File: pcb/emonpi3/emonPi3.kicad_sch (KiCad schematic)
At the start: 133 parts, among them CN1 CONN_03SCREW, CN2 CONN_03SCREW, CN3 CONN_03SCREW, J10 Conn_ARM_JTAG_SWD_10, J11 Conn_02x13_Odd_Even, J12 PINHD-1X9, J7 CONN_04PTH, J8 CONN_04PTH, J9 USB_C_Receptacle_USB2.0, SW1 SW_Push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

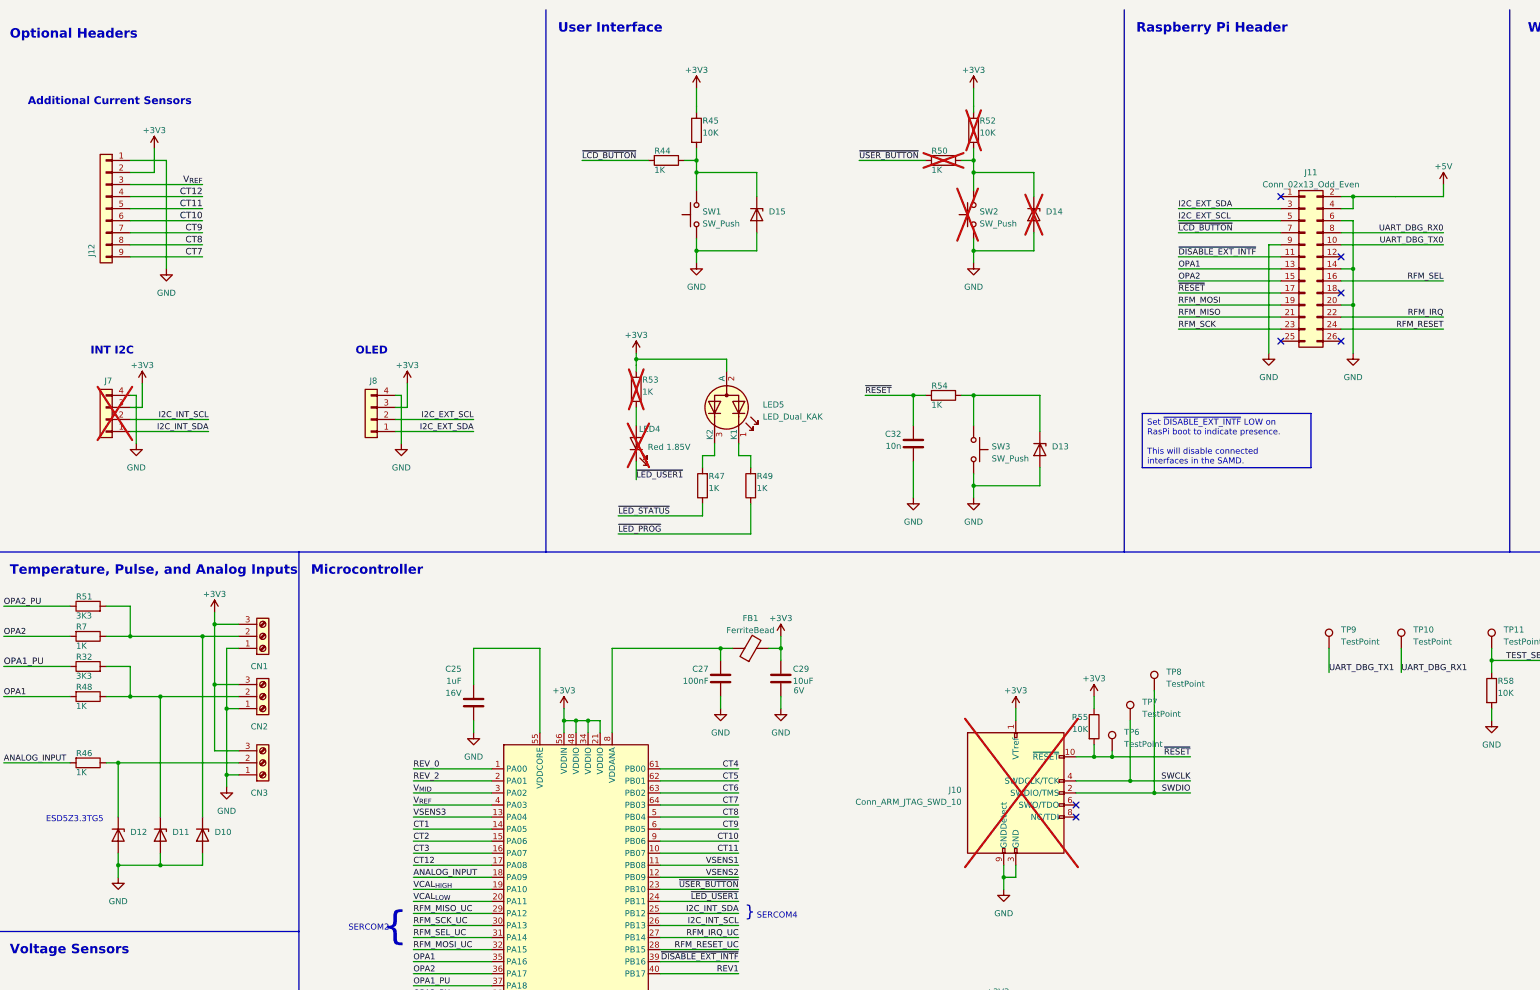
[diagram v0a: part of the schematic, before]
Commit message: * [Header] Use 40 pin RasPi header and move 6CT header
  - Use a 40 pin header for RasPi
  - Move 6CT (and change pinout) to allow this
  - Use routing mapping for CT inputs, do remap in software
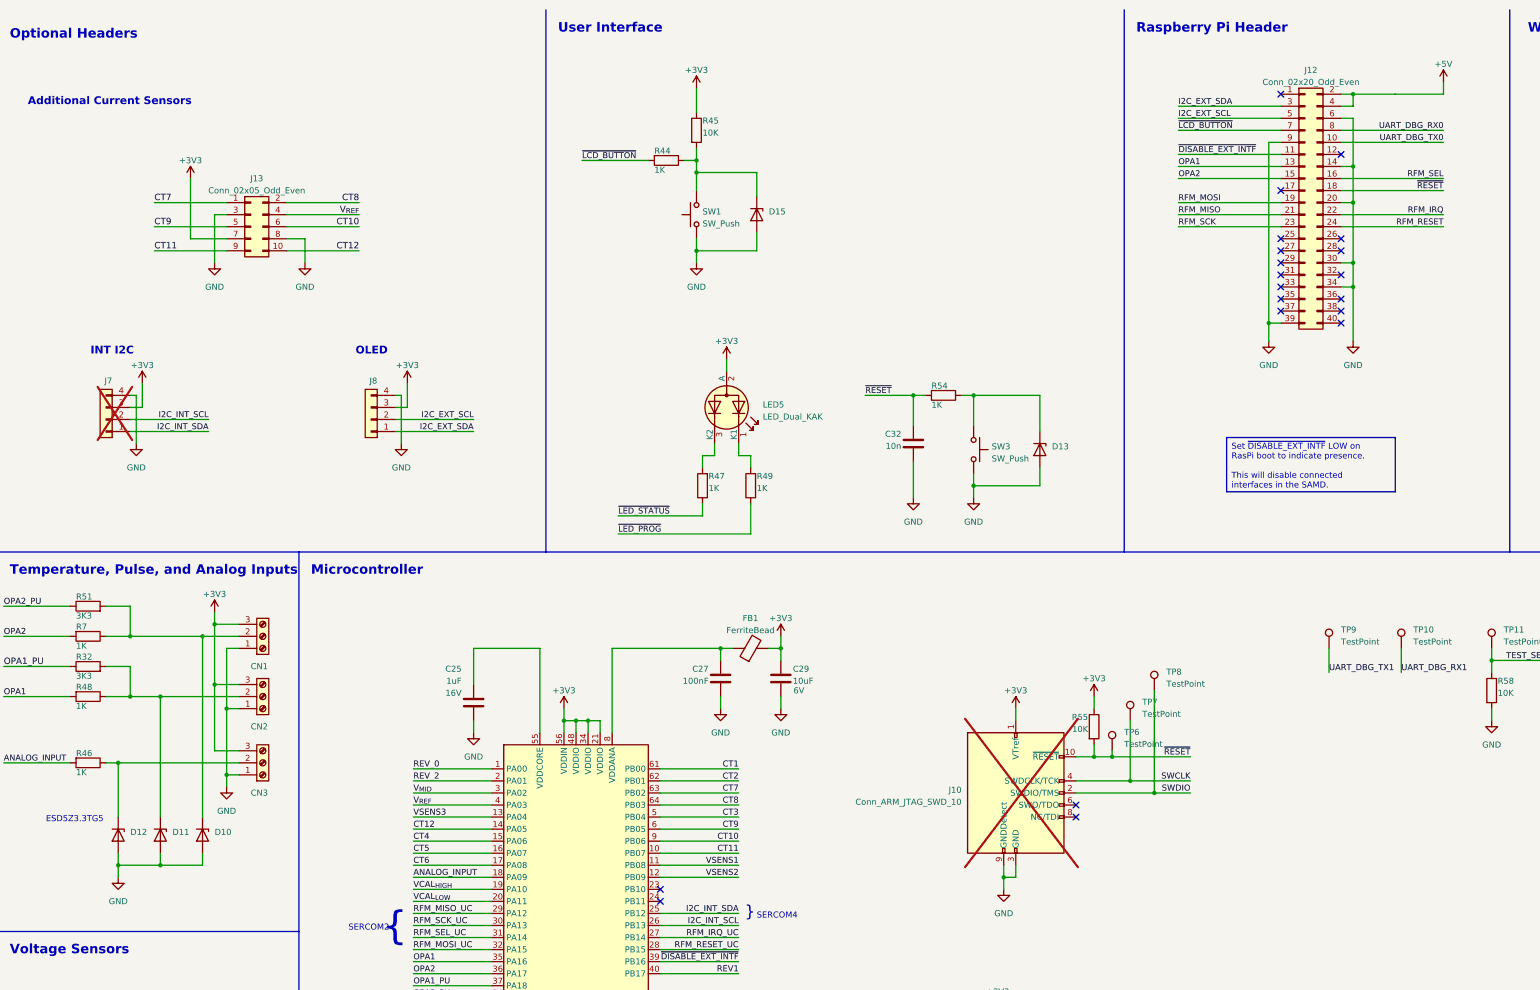
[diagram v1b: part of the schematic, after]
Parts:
- removed D14: ESD5Z3.3T5G, Diode_SMD:D_SOD-523, symbol Diode:ESD5Zxx
- removed J11: Conn_02x13_Odd_Even, RPi-SMD:REF-182688, symbol Connector_Generic:Conn_02x13_Odd_Even
- removed J12: PINHD-1X9, Connector_PinSocket_2.54mm:PinSocket_1x09_P2.54mm_Vertical, symbol Connector_Generic:Conn_01x09
- removed LED4: Red 1.85V, LED_SMD:LED_0805_2012Metric, symbol Device:LED
- removed R50, R53: 1K, Resistor_SMD:R_0603_1608Metric, symbol Device:R
- removed R52: 10K, Resistor_SMD:R_0603_1608Metric, symbol Device:R
- removed SW2: SW_Push, Button_Switch_THT:SW_PUSH_6mm, symbol Switch:SW_Push
- added J12: Conn_02x20_Odd_Even, RPi-SMD:REF-182665, symbol Connector_Generic:Conn_02x20_Odd_Even
- added J13: Conn_02x05_Odd_Even, Connector_PinSocket_2.54mm:PinSocket_2x05_P2.54mm_Vertical, symbol Connector_Generic:Conn_02x05_Odd_Even
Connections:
- net +3V3: now also J13.7 (Pin_7)
- net +5V: now also J12.2 (Pin_2), J12.4 (Pin_4)
- net CT1: now also U3.61 (PB00); no longer U3.14 (PA05)
- net CT10: now also J13.6 (Pin_6)
- net CT11: now also J13.9 (Pin_9)
- net CT12: now also U3.14 (PA05), J13.10 (Pin_10); no longer U3.17 (PA08)
- net CT2: now also U3.62 (PB01); no longer U3.15 (PA06)
- net CT3: now also U3.5 (PB04); no longer U3.16 (PA07)
- net CT4: now also U3.15 (PA06); no longer U3.61 (PB00)
- net CT5: now also U3.16 (PA07); no longer U3.62 (PB01)
- net CT6: now also U3.17 (PA08); no longer U3.63 (PB02)
- net CT7: now also U3.63 (PB02), J13.1 (Pin_1); no longer U3.64 (PB03)
- net CT8: now also U3.64 (PB03), J13.2 (Pin_2); no longer U3.5 (PB04)
- net CT9: now also J13.5 (Pin_5)
- net GND: now also J12.14 (Pin_14), J12.20 (Pin_20), J12.30 (Pin_30), J12.34 (Pin_34), J12.39 (Pin_39), J12.6 (Pin_6), J12.9 (Pin_9), J13.3 (Pin_3), J13.8 (Pin_8)
- net I2C_EXT_SCL: now also J12.5 (Pin_5)
- net I2C_EXT_SDA: now also J12.3 (Pin_3)
- net OPA1: now also J12.13 (Pin_13)
- net OPA2: now also J12.15 (Pin_15)
- net RFM_IRQ: now also J12.22 (Pin_22)
- net RFM_MISO: now also J12.21 (Pin_21)
- net RFM_MOSI: now also J12.19 (Pin_19)
- net RFM_RESET: now also J12.24 (Pin_24)
- net RFM_SCK: now also J12.23 (Pin_23)
- net RFM_SEL: now also J12.16 (Pin_16)
- net UART_DBG_RX0: now also J12.8 (Pin_8)
- net UART_DBG_TX0: now also J12.10 (Pin_10)
- net V_{REF}: now also J13.4 (Pin_4)
- net ~{DISABLE_EXT_INTF}: now also J12.11 (Pin_11)
- net ~{LCD_BUTTON}: now also J12.7 (Pin_7)
- net ~{RESET}: now also J12.18 (Pin_18)
- net ~{LED_USER1}: no longer names the net of U3.24 (PB11)
- net ~{USER_BUTTON}: no longer names the net of U3.23 (PB10)
- no-connect marks 14 -> 27

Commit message: * Changes for manufacture
  - Better silkscreen naming
  - Move test points to top layer and remove alignment holes
  - Remove additional UART pads
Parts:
- removed CN1, CN2: CONN_03SCREW, TerminalBlock_Phoenix:TerminalBlock_Phoenix_PT-1,5-3-3.5-H_1x03_P3.50mm_Horizontal, symbol Connector:Screw_Terminal_01x03
- removed H5, H6: MountingHole, MountingHole:MountingHole_2.1mm, symbol Mechanical:MountingHole
- removed R58: 10K, Resistor_SMD:R_0603_1608Metric, symbol Device:R
- removed TP10, TP11, TP7, TP8, TP9: TestPoint, TestPoint:TestPoint_Pad_D1.0mm, symbol Connector:TestPoint
- added CN1: Screw_Terminal_01x06, TerminalBlock_Phoenix:TerminalBlock_Phoenix_PT-1,5-6-3.5-H_1x06_P3.50mm_Horizontal, symbol Connector:Screw_Terminal_01x06
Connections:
- net +3V3: now also CN1.3 (Pin_3), CN1.6 (Pin_6)
- net GND: now also TP6.1, CN1.1 (Pin_1), CN1.4 (Pin_4)
- net ~{RESET}: no longer TP6.1
- net at D10.1 (K), R51.2, R7.1: now also CN1.5 (Pin_5)
- net at D11.1 (K), R32.2, R48.1: now also CN1.2 (Pin_2)
- net TEST_SENSE: no longer names the net of U3.53 (PA28)
- net UART_DBG_RX1: no longer names the net of U3.60 (PB31)
- net UART_DBG_TX1: no longer names the net of U3.59 (PB30)
- no-connect marks 27 -> 30
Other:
- moved on the sheet: H7

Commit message: * More refinement
  - Add TPS2116 model
  - Remove ground slivers
  - 50R trace for RFM output
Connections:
- net +3V3: now also R63.2
- net at C40.1, FB2.2, U7.2 (VDD): no longer R63.2
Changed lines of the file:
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@@
   (junction (at 74.93 76.2) (diameter 0) (color 0 0 0 0)
   )
-  (junction (at 508 54.61) (diameter 0) (color 0 0 0 0)
-  )
   (junction (at 251.46 344.17) (diameter 0) (color 0 0 0 0)
   )
@@
     (stroke (width 0) (type default))
   )
-  (wire (pts (xy 508 54.61) (xy 508 43.18))
-    (stroke (width 0) (type default))
-  )
   (wire (pts (xy 360.68 226.06) (xy 374.65 226.06))
     (stroke (width 0) (type default))
@@
     (stroke (width 0) (type default))
   )
-  (wire (pts (xy 495.3 43.18) (xy 508 43.18))
-    (stroke (width 0) (type default))
-  )
   (wire (pts (xy 181.61 142.24) (xy 186.69 142.24))
     (stroke (width 0) (type default))
@@
     (stroke (width 0) (type default))
   )
-  (wire (pts (xy 508 57.15) (xy 508 54.61))
-    (stroke (width 0) (type default))
-  )
   (wire (pts (xy 532.13 255.27) (xy 537.21 255.27))
     (stroke (width 0) (type default))
@@
     (stroke (width 0) (type default))
   )
-  (wire (pts (xy 511.81 54.61) (xy 511.81 59.69))
+  (wire (pts (xy 511.81 43.18) (xy 511.81 59.69))
     (stroke (width 0) (type default))
   )
@@
     (stroke (width 0.1524) (type solid))
   )
-  (wire (pts (xy 508 54.61) (xy 511.81 54.61))
+  (wire (pts (xy 495.3 43.18) (xy 511.81 43.18))
     (stroke (width 0) (type default))
   )
@@
     (stroke (width 0) (type default))
   )
+  (wire (pts (xy 508 54.61) (xy 508 57.15))
+    (stroke (width 0) (type default))
+  )
   (wire (pts (xy 502.92 72.39) (xy 514.35 72.39))
     (stroke (width 0) (type default))
@@
         )
       )
+    )
+  )
+  (symbol (lib_id "power:+3V3") (at 508 54.61 0) (unit 1)
+    (in_bom yes) (on_board yes) (dnp no) (fields_autoplaced)
+    (property "Reference" "#PWR040" (at 508 58.42 0)
+      (effects (font (size 1.27 1.27)) hide)
+    )
+    (property "Value" "+3V3" (at 508 50.8 0)
+      (effects (font (size 1.27 1.27)))
+    )
+    (property "Footprint" "" (at 508 54.61 0)
+      (effects (font (size 1.27 1.27)) hide)
+    )
+    (property "Datasheet" "" (at 508 54.61 0)
+      (effects (font (size 1.27 1.27)) hide)
+    )
+    (pin "1")
+    (instances
+      (project "emonPi3"
+        (path "/3a5f1087-1abe-4575-9313-bd86a5e03366"
+          (reference "#PWR040") (unit 1)
+        )
+      )

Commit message: * [v0.2] Final touches for manufacture
  - Remove h/w zero crossing
  - Adjust hole spacing for CT expander
  - Add teardrops
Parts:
- removed C39: 100nF, Capacitor_SMD:C_0603_1608Metric, symbol Device:C
- removed R64, R65: 47K, Resistor_SMD:R_0603_1608Metric, symbol Device:R
- removed R68: 1M, Resistor_SMD:R_0603_1608Metric, symbol Device:R
- removed R69: 10K, Resistor_SMD:R_0603_1608Metric, symbol Device:R
- removed U6: MCP6546U, Package_TO_SOT_SMD:SOT-23-5, symbol Comparator:LMV331
- R32, R39, R40, R41, R51, R66, R67: value 3K3 -> 3K0
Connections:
- net VSENS_{POL}: no longer names the net of U3.51 (PA27)
- no-connect marks 30 -> 31
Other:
- note removed: "Zero Crossing Detector"
